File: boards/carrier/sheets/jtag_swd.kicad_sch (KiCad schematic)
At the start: 4 parts

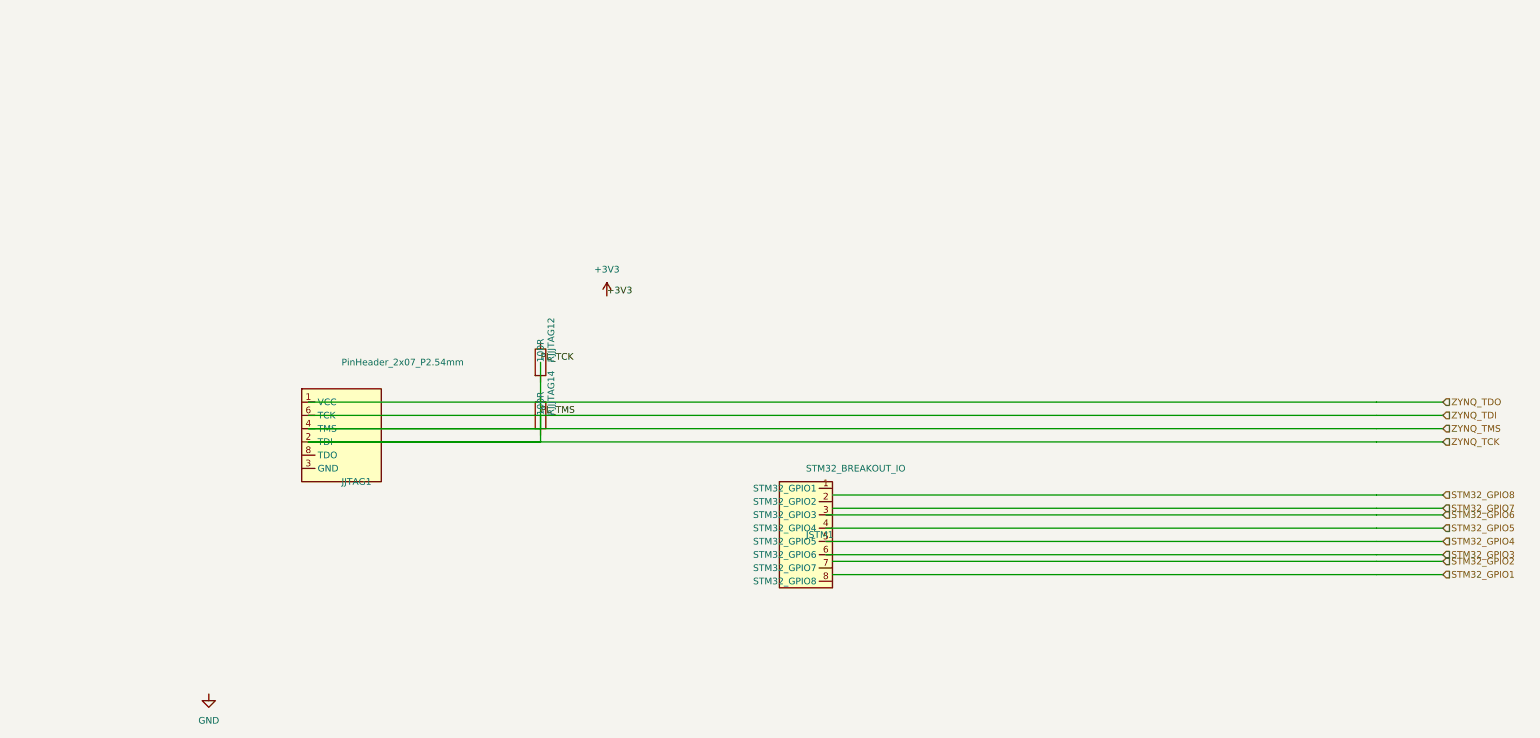
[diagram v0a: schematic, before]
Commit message: Stage 6 (2/4): add microsd, boot_switches, jtag_swd blocks (skip aux_io, xadc_clk)
  * microsd: Hirose DM3AT-SF-PEJM5 push-push socket on Zynq PS SD1 (4-bit
    SDIO + dedicated card-detect via DET_A/DET_B). Uses KiCad built-in
    Connector:Micro_SD_Card_Det_Hirose_DM3AT symbol; VDD decoupling and
    DAT[0..3]/CMD pull-ups come from MICROSD_DM3AT_REFCIRCUIT.

  * boot_switches: SW1 4-pos DIP (ZYNQ_BOOT_MODE[3:0] straps with 10k
    pull-ups from DIP_SWITCH_REFCIRCUIT) + SW2 tactile (ZYNQ_PS_SRST_N
    with pull-up + debounce from TACTILE_SWITCH_REFCIRCUIT).

  * jtag_swd: J1 Zynq PS JTAG 2x7 (UG470 Xilinx 6-wire pinout, no TRST
    pin in the JTAG_2x7 symbol) + J2 STM32 SWD 2x5 (ARM Cortex 10-pin
    with SWDIO/nRESET pull-ups from SWD_HEADER_REFCIRCUIT).

  * aux_io and xadc_clk skipped: no refcircuit exists for AUX_GPIO_IO
    or XADC_MRCC_IO connectors, and authoring new refcircuits is
    out of scope per task instructions.

$ python -m zynq_eda --board carrier
built 5 block(s): power, usb_pd, microsd, boot_switches, jtag_swd

Co-Authored-By: Claude Opus 4.7 <noreply@anthropic.com>
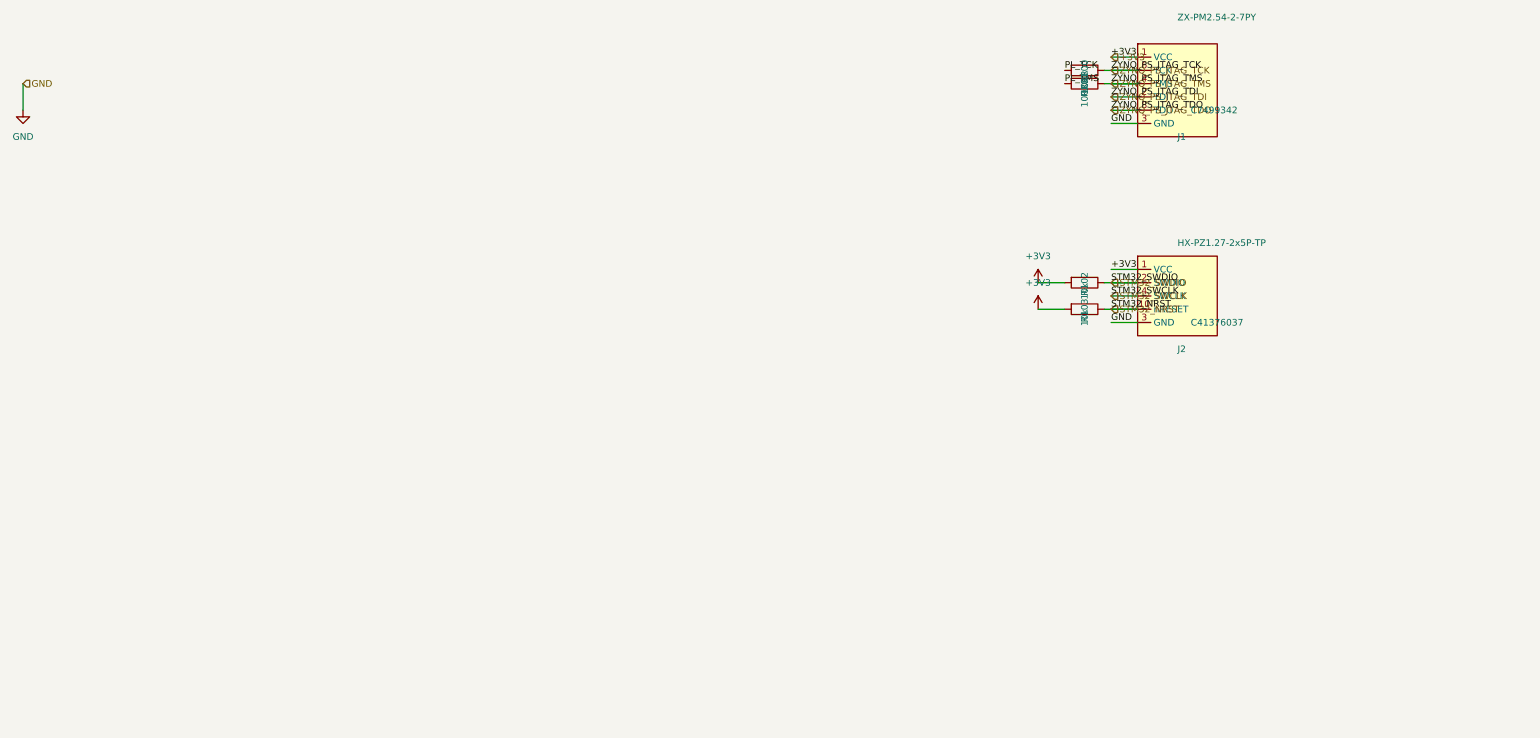
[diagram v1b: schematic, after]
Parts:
- removed JJTAG1: PinHeader_2x07_P2.54mm, Connector_PinHeader_2.54mm:PinHeader_2x07_P2.54mm_Vertical, symbol carrier:JTAG_2x7
- removed JSTM1: STM32_BREAKOUT_IO, symbol STM32_BREAKOUT_IO:STM32_BREAKOUT_IO
- removed RJJJTAG12, RJJJTAG14: 100R, Resistor_SMD:R_0402_1005Metric, symbol Device:R
- added J1: ZX-PM2.54-2-7PY, Connector_PinHeader_2.54mm:PinHeader_2x07_P2.54mm_Vertical, symbol zynq_eda:JTAG_2x7
- added J2: HX-PZ1.27-2x5P-TP, Connector_PinHeader_1.27mm:PinHeader_2x05_P1.27mm_Vertical, symbol zynq_eda:SWD_2x5
- added R100, R101: 100R, Resistor_SMD:R_0402_1005Metric, symbol Device:R
- added R102, R103: 10k, Resistor_SMD:R_0402_1005Metric, symbol Device:R
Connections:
- net +3V3: now also J1.1 (VCC), J2.1 (VCC), R102.2, R103.2
- net GND: now also J1.3 (GND), J2.3 (GND)
- new net PL_TCK: R100.2
- new net PL_TMS: R101.2
- new net STM32_NRST: J2.10 (nRESET), R103.1
- new net STM32_SWCLK: J2.4 (SWCLK)
- new net STM32_SWDIO: J2.2 (SWDIO), R102.1
- new net ZYNQ_PS_JTAG_TCK: J1.6 (TCK), R100.1
- new net ZYNQ_PS_JTAG_TDI: J1.2 (TDI)
- new net ZYNQ_PS_JTAG_TDO: J1.8 (TDO)
- new net ZYNQ_PS_JTAG_TMS: J1.4 (TMS), R101.1
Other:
- title: JTAG + STM32 Breakout -> Debug Headers (Zynq PS JTAG 2x7 + STM32 SWD 2x5)
